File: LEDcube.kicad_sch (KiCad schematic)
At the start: 26 parts, among them J101 IN, J102 OUT, J103 JTAG, U101 AP1117-33, U102 STM32F030F4Px, U103 SP3485CN, Y101 16MHz

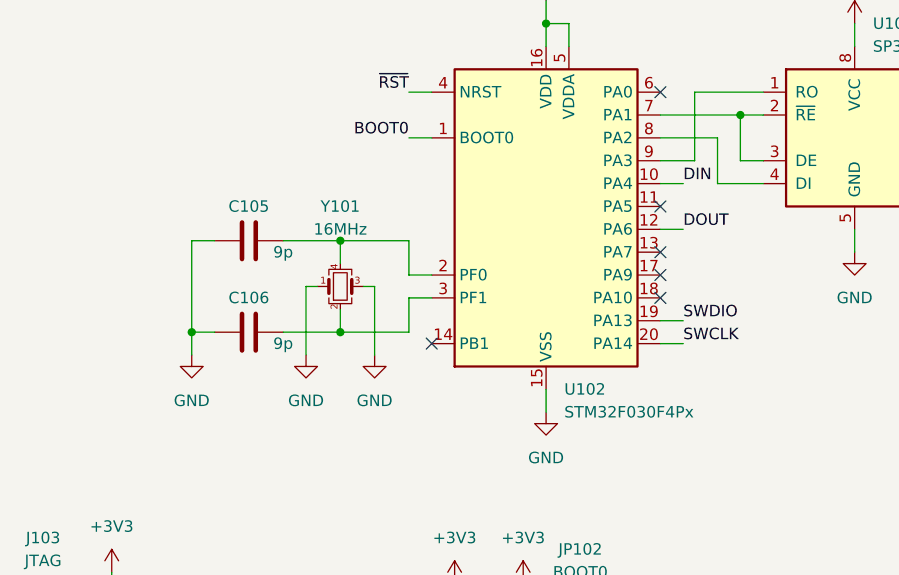
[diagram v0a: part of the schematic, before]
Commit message: Crystal related fixes
Signed-off-by: Benedikt Spranger <b.spranger@linutronix.de>
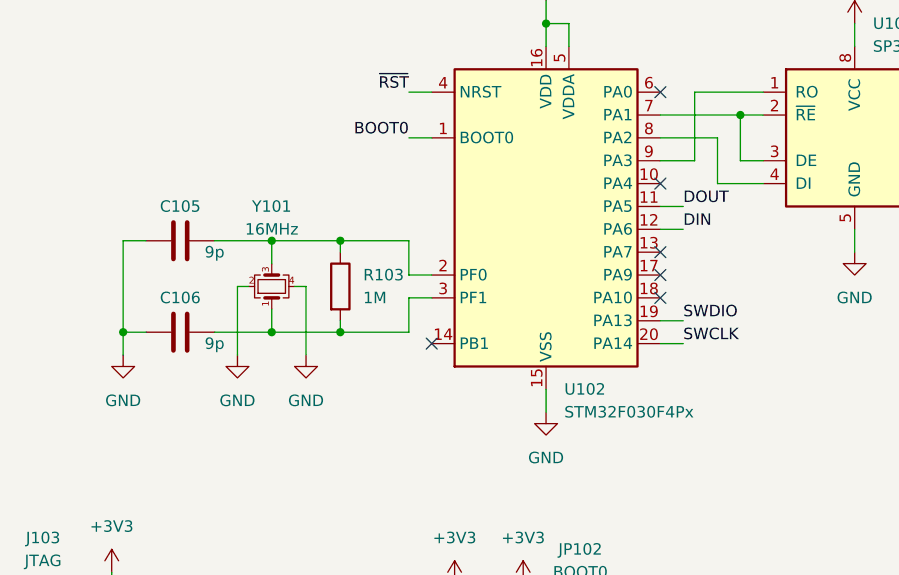
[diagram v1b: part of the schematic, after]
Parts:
- added R103: 1M, Resistor_SMD:R_0402_1005Metric, symbol Device:R
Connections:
- net DIN: now also U102.12 (PA6); no longer U102.10 (PA4)
- net DOUT: now also U102.11 (PA5); no longer U102.12 (PA6)
- net GND: now also Y101.2, Y101.4; no longer Y101.1, Y101.3
- net at C106.2, U102.3 (PF1): now also Y101.1, R103.2; no longer Y101.2
- net at C105.2, U102.2 (PF0): now also Y101.3, R103.1; no longer Y101.4
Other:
- moved on the sheet: C105, C106, Y101
